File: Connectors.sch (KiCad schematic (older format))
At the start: 12 parts, among them J10 JST-PH, J11 USB_C_Receptacle_USB2.0, J9 Micro_SD_Card_Det, U8 USBLC6-2SC6

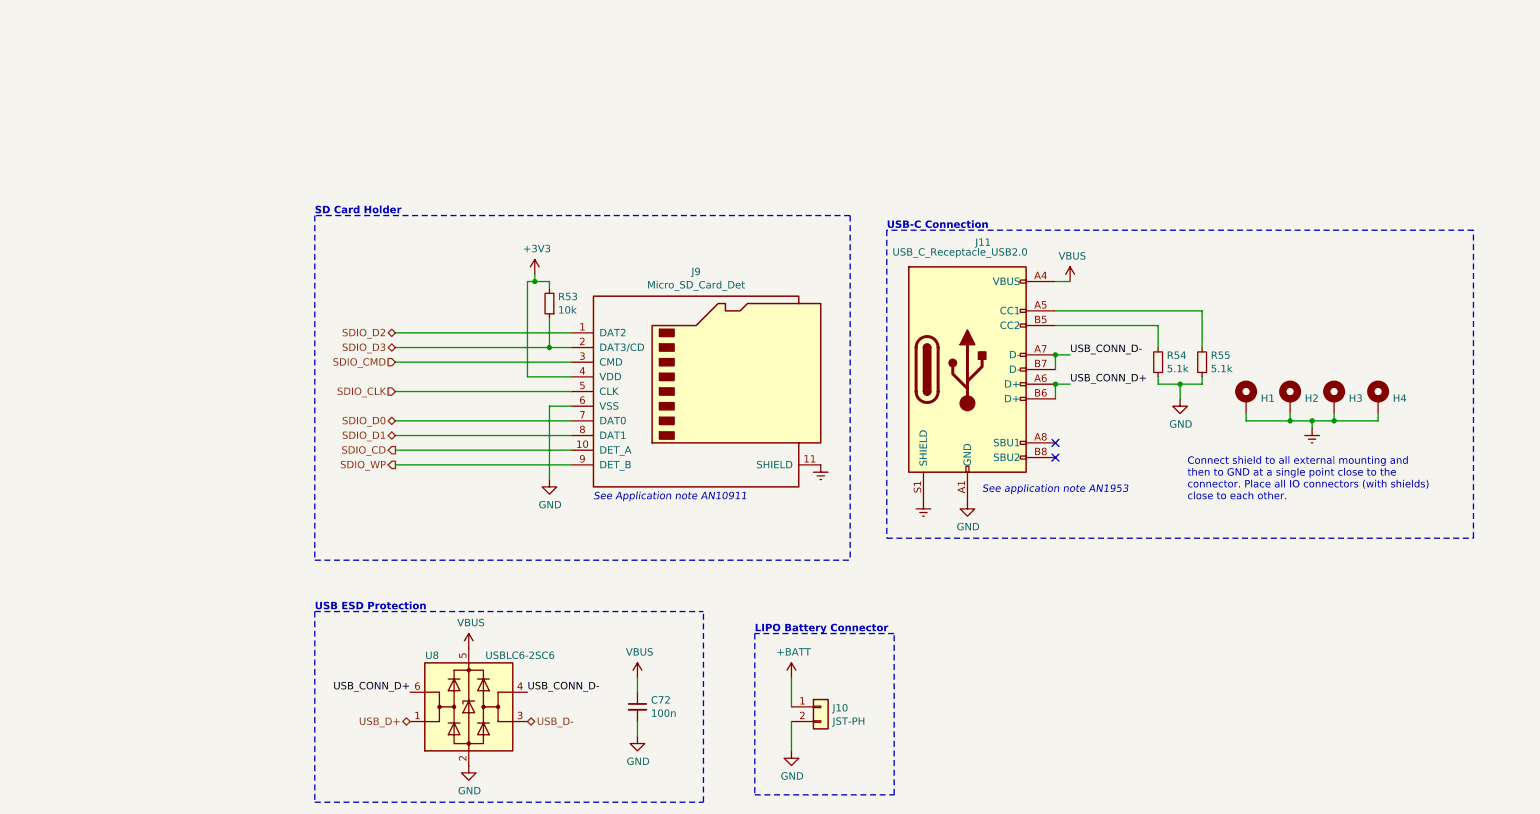
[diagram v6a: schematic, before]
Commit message: Assign footprints for all components
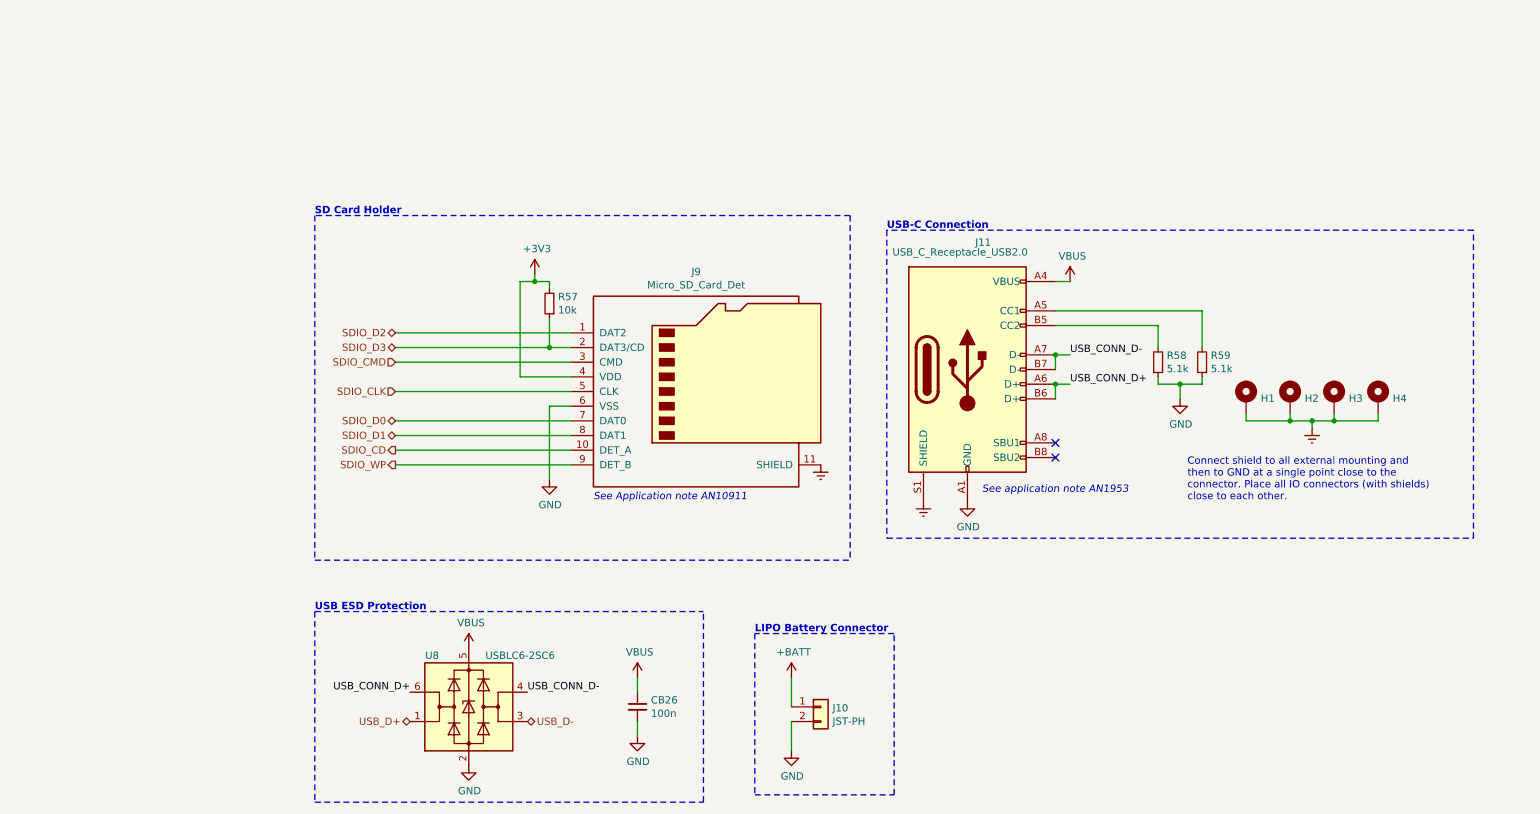
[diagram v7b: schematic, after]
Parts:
- CB26: renamed from C72; footprint (none) -> Capacitor_SMD:C_0603_1608Metric_Pad1.05x0.95mm_HandSolder
- H1, H2, H3, H4: footprint (none) -> MountingHole:MountingHole_4.3mm_M4_Pad_Via
- J10: footprint (none) -> Connector_JST:JST_PH_S2B-PH-SM4-TB_1x02-1MP_P2.00mm_Horizontal; MPN (none) -> 1769; Mfr. (none) -> Adafruit
- J11: footprint (none) -> grootvoet:USB_C_Receptacle_Amphenol_12401610E4-2A; MPN DX07S016JA1R1500 -> 12401610E4#2A; Mfr. JAE Electronics -> Amphenol Commercial Products
- J9: footprint (none) -> Connector_Card:microSD_HC_Hirose_DM3D-SF; MPN (none) -> DM3D-SF; Mfr. (none) -> Hirose Connector
- R57: renamed from R53; footprint (none) -> Resistor_SMD:R_0603_1608Metric_Pad1.05x0.95mm_HandSolder
- R58: renamed from R54; footprint (none) -> Resistor_SMD:R_0603_1608Metric_Pad1.05x0.95mm_HandSolder
- R59: renamed from R55; footprint (none) -> Resistor_SMD:R_0603_1608Metric_Pad1.05x0.95mm_HandSolder
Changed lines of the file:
@@
 $EndDescr
 $Comp
-L power:GND #PWR095
+L power:GND #PWR0116
 U 1 1 5EF579E9
 P 7200 4000
-F 0 "#PWR095" H 7200 3750 50  0001 C CNN
+F 0 "#PWR0116" H 7200 3750 50  0001 C CNN
 F 1 "GND" H 7205 3827 50  0000 C CNN
 F 2 "" H 7200 4000 50  0001 C CNN
@@
 $EndComp
 $Comp
-L power:Earth #PWR094
+L power:Earth #PWR0115
 U 1 1 5EF579EF
 P 6900 4000
-F 0 "#PWR094" H 6900 3750 50  0001 C CNN
+F 0 "#PWR0115" H 6900 3750 50  0001 C CNN
 F 1 "Earth" H 6900 3850 50  0001 C CNN
 F 2 "" H 6900 4000 50  0001 C CNN
@@
 $EndComp
 $Comp
-L power:VBUS #PWR096
+L power:VBUS #PWR0117
 U 1 1 5EF579F5
 P 7900 2500
-F 0 "#PWR096" H 7900 2350 50  0001 C CNN
+F 0 "#PWR0117" H 7900 2350 50  0001 C CNN
 F 1 "VBUS" H 7915 2673 50  0000 C CNN
 F 2 "" H 7900 2500 50  0001 C CNN
@@
 F 0 "J11" H 7307 3967 50  0000 C CNN
 F 1 "USB_C_Receptacle_USB2.0" H 7150 3900 50  0000 C CNN
-F 2 "" H 7350 3100 50  0001 C CNN
+F 2 "grootvoet:USB_C_Receptacle_Amphenol_12401610E4-2A" H 7350 3100 50  0001 C CNN
 F 3 "https://www.usb.org/sites/default/files/documents/usb_type-c.zip" H 7350 3100 50  0001 C CNN
-F 4 "JAE Electronics" H 7200 3100 50  0001 C CNN "Mfr."
-F 5 "DX07S016JA1R1500" H 7200 3100 50  0001 C CNN "MPN"
+F 4 "Amphenol Commercial Products" H 7200 3100 50  0001 C CNN "Mfr."
+F 5 "12401610E4#2A" H 7200 3100 50  0001 C CNN "MPN"
 	1    7200 3100
 	1    0    0    -1
@@
 NoConn ~ 7800 3600
 $Comp
-L Device:R_Small R54
+L Device:R_Small R58
 U 1 1 5EF57A0A
 P 8500 3050
-F 0 "R54" H 8441 3004 50  0000 R CNN
+F 0 "R58" H 8441 3004 50  0000 R CNN
 F 1 "5.1k" H 8441 3095 50  0000 R CNN
-F 2 "" H 8500 3050 50  0001 C CNN
+F 2 "Resistor_SMD:R_0603_1608Metric_Pad1.05x0.95mm_HandSolder" H 8500 3050 50  0001 C CNN
 F 3 "~" H 8500 3050 50  0001 C CNN
 	1    8500 3050
@@
 $EndComp
 $Comp
-L Device:R_Small R55
+L Device:R_Small R59
 U 1 1 5EF57A10
 P 8800 3050
-F 0 "R55" H 8741 3004 50  0000 R CNN
+F 0 "R59" H 8741 3004 50  0000 R CNN
 F 1 "5.1k" H 8741 3095 50  0000 R CNN
-F 2 "" H 8800 3050 50  0001 C CNN
+F 2 "Resistor_SMD:R_0603_1608Metric_Pad1.05x0.95mm_HandSolder" H 8800 3050 50  0001 C CNN
 F 3 "~" H 8800 3050 50  0001 C CNN
 	1    8800 3050
@@
 	8800 2700 7800 2700
 $Comp
-L power:GND #PWR097
+L power:GND #PWR0118
 U 1 1 5EF57A1A
 P 8650 3300
-F 0 "#PWR097" H 8650 3050 50  0001 C CNN
+F 0 "#PWR0118" H 8650 3050 50  0001 C CNN
 F 1 "GND" H 8655 3127 50  0000 C CNN
 F 2 "" H 8650 3300 50  0001 C CNN
@@
 	9550 3500 9550 3450
 $Comp
-L power:Earth #PWR098
+L power:Earth #PWR0119
 U 1 1 5EF57A38
 P 9550 3500
-F 0 "#PWR098" H 9550 3250 50  0001 C CNN
+F 0 "#PWR0119" H 9550 3250 50  0001 C CNN
 F 1 "Earth" H 9550 3350 50  0001 C CNN
 F 2 "" H 9550 3500 50  0001 C CNN
@@
 F 0 "H4" H 10100 3303 50  0000 L CNN
 F 1 "MountingHole_Pad" H 10100 3258 50  0001 L CNN
-F 2 "" H 10000 3300 50  0001 C CNN
+F 2 "MountingHole:MountingHole_4.3mm_M4_Pad_Via" H 10000 3300 50  0001 C CNN
 F 3 "~" H 10000 3300 50  0001 C CNN
 	1    10000 3300
@@
 F 0 "H3" H 9800 3303 50  0000 L CNN
 F 1 "MountingHole_Pad" H 9800 3258 50  0001 L CNN
-F 2 "" H 9700 3300 50  0001 C CNN
+F 2 "MountingHole:MountingHole_4.3mm_M4_Pad_Via" H 9700 3300 50  0001 C CNN
 F 3 "~" H 9700 3300 50  0001 C CNN
 	1    9700 3300
@@
 F 0 "H2" H 9500 3303 50  0000 L CNN
 F 1 "MountingHole_Pad" H 9500 3258 50  0001 L CNN
-F 2 "" H 9400 3300 50  0001 C CNN
+F 2 "MountingHole:MountingHole_4.3mm_M4_Pad_Via" H 9400 3300 50  0001 C CNN
 F 3 "~" H 9400 3300 50  0001 C CNN
 	1    9400 3300
@@
 F 0 "H1" H 9200 3303 50  0000 L CNN
 F 1 "MountingHole_Pad" H 9200 3258 50  0001 L CNN
-F 2 "" H 9100 3300 50  0001 C CNN
+F 2 "MountingHole:MountingHole_4.3mm_M4_Pad_Via" H 9100 3300 50  0001 C CNN
 F 3 "~" H 9100 3300 50  0001 C CNN
 	1    9100 3300
@@
 USB-C Connection
 $Comp
-L power:Earth #PWR093
+L power:Earth #PWR0114
 U 1 1 5EF59730
 P 6200 3750
-F 0 "#PWR093" H 6200 3500 50  0001 C CNN
+F 0 "#PWR0114" H 6200 3500 50  0001 C CNN
 F 1 "Earth" H 6200 3600 50  0001 C CNN
 F 2 "" H 6200 3750 50  0001 C CNN
@@
 Text Notes 4650 4000 0    50   Italic 0
 See Application note AN10911
-Wire Wire Line
-	4500 3150 4200 3150
 Text HLabel 3300 3750 0    50   Output ~ 0
 SDIO_WP
 $Comp
-L power:GND #PWR088
+L power:GND #PWR0109
 U 1 1 5EFBCDAD
 P 4350 3850
-F 0 "#PWR088" H 4350 3600 50  0001 C CNN
+F 0 "#PWR0109" H 4350 3600 50  0001 C CNN
 F 1 "GND" H 4355 3677 50  0000 C CNN
 F 2 "" H 4350 3850 50  0001 C CNN
@@
 F 0 "J10" H 6280 5392 50  0000 L CNN
 F 1 "JST-PH" H 6280 5301 50  0000 L CNN
-F 2 "" H 6200 5400 50  0001 C CNN
+F 2 "Connector_JST:JST_PH_S2B-PH-SM4-TB_1x02-1MP_P2.00mm_Horizontal" H 6200 5400 50  0001 C CNN
 F 3 "~" H 6200 5400 50  0001 C CNN
+F 4 "1769" H 6200 5400 50  0001 C CNN "MPN"
+F 5 "Adafruit" H 6200 5400 50  0001 C CNN "Mfr."
 	1    6200 5400
 	1    0    0    -1
 $EndComp
 $Comp
-L power:+BATT #PWR091
+L power:+BATT #PWR0112
 U 1 1 5EE0C94B
 P 6000 5200
-F 0 "#PWR091" H 6000 5050 50  0001 C CNN
+F 0 "#PWR0112" H 6000 5050 50  0001 C CNN
 F 1 "+BATT" H 6015 5373 50  0000 C CNN
 F 2 "" H 6000 5200 50  0001 C CNN
@@
 $EndComp
 $Comp
-L power:GND #PWR092
+L power:GND #PWR0113
 U 1 1 5EE0C951
 P 6000 5700
-F 0 "#PWR092" H 6000 5450 50  0001 C CNN
+F 0 "#PWR0113" H 6000 5450 50  0001 C CNN
 F 1 "GND" H 6005 5527 50  0000 C CNN
 F 2 "" H 6000 5700 50  0001 C CNN
@@
 $EndComp
 $Comp
-L power:GND #PWR086
+L power:GND #PWR0107
 U 1 1 5EF9E21E
 P 3800 5800
-F 0 "#PWR086" H 3800 5550 50  0001 C CNN
+F 0 "#PWR0107" H 3800 5550 50  0001 C CNN
 F 1 "GND" H 3805 5627 50  0000 C CNN
 F 2 "" H 3800 5800 50  0001 C CNN
@@
 $EndComp
 $Comp
-L power:VBUS #PWR085
+L power:VBUS #PWR0106
 U 1 1 5EF9EE8C
 P 3800 5000
-F 0 "#PWR085" H 3800 4850 50  0001 C CNN
+F 0 "#PWR0106" H 3800 4850 50  0001 C CNN
 F 1 "VBUS" H 3815 5173 50  0000 C CNN
 F 2 "" H 3800 5000 50  0001 C CNN
@@
 USB ESD Protection
 $Comp
-L Device:C_Small C72
+L Device:C_Small CB26
 U 1 1 5EFBCA6D
 P 4950 5400
-F 0 "C72" H 5042 5446 50  0000 L CNN
+F 0 "CB26" H 5042 5446 50  0000 L CNN
 F 1 "100n" H 5042 5355 50  0000 L CNN
-F 2 "" H 4950 5400 50  0001 C CNN
+F 2 "Capacitor_SMD:C_0603_1608Metric_Pad1.05x0.95mm_HandSolder" H 4950 5400 50  0001 C CNN
 F 3 "~" H 4950 5400 50  0001 C CNN
 	1    4950 5400
@@
 $EndComp
 $Comp
-L power:VBUS #PWR089
+L power:VBUS #PWR0110
 U 1 1 5EFBD2C9
 P 4950 5200
-F 0 "#PWR089" H 4950 5050 50  0001 C CNN
+F 0 "#PWR0110" H 4950 5050 50  0001 C CNN
 F 1 "VBUS" H 4965 5373 50  0000 C CNN
 F 2 "" H 4950 5200 50  0001 C CNN
@@
 $EndComp
 $Comp
-L power:GND #PWR090
+L power:GND #PWR0111
 U 1 1 5EFBD729
 P 4950 5600
-F 0 "#PWR090" H 4950 5350 50  0001 C CNN
+F 0 "#PWR0111" H 4950 5350 50  0001 C CNN
 F 1 "GND" H 4955 5427 50  0000 C CNN
 F 2 "" H 4950 5600 50  0001 C CNN
@@
 	2750 4750 5400 4750
 $Comp
-L Device:R_Small R53
+L Device:R_Small R57
 U 1 1 5EF7DC5F
 P 4350 2650
-F 0 "R53" H 4291 2604 50  0000 R CNN
+F 0 "R57" H 4291 2604 50  0000 R CNN
 F 1 "10k" H 4291 2695 50  0000 R CNN
-F 2 "" H 4350 2650 50  0001 C CNN
+F 2 "Resistor_SMD:R_0603_1608Metric_Pad1.05x0.95mm_HandSolder" H 4350 2650 50  0001 C CNN
 F 3 "~" H 4350 2650 50  0001 C CNN
 	1    4350 2650
@@
 F 0 "J9" H 5350 4067 50  0000 C CNN
 F 1 "Micro_SD_Card_Det" H 5350 3976 50  0000 C CNN
-F 2 "" H 7450 3950 50  0001 C CNN
+F 2 "Connector_Card:microSD_HC_Hirose_DM3D-SF" H 7450 3950 50  0001 C CNN
 F 3 "https://www.hirose.com/product/en/download_file/key_name/DM3/category/Catalog/doc_file_id/49662/?file_category_id=4&item_id=195&is_series=1" H 5400 3350 50  0001 C CNN
+F 4 "DM3D-SF" H 5400 3250 50  0001 C CNN "MPN"
+F 5 "Hirose Connector" H 5400 3250 50  0001 C CNN "Mfr."
 	1    5400 3250
 	1    0    0    -1
 $EndComp
 $Comp
-L power:+3V3 #PWR087
+L power:+3V3 #PWR0108
 U 1 1 5EF922F3
 P 4250 2450
-F 0 "#PWR087" H 4250 2300 50  0001 C CNN
+F 0 "#PWR0108" H 4250 2300 50  0001 C CNN
 F 1 "+3V3" H 4265 2623 50  0000 C CNN
 F 2 "" H 4250 2450 50  0001 C CNN
@@
 	4250 2500 4250 2450
 Wire Wire Line
-	4250 2500 4200 2500
-Wire Wire Line
-	4200 2500 4200 3150
+	4150 2500 4150 3150
 Connection ~ 4250 2500
+Wire Wire Line
+	4150 2500 4250 2500
+Wire Wire Line
+	4150 3150 4500 3150
 $EndSCHEMATC
